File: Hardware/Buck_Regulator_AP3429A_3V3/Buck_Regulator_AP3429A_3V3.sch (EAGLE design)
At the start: 28 parts, among them J1 Screw Terminal, J2 POWER_JACKPOWER_JACK_SLOT_COM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, J3 Breakout Headers, U1 AP3429/A

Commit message: Updates from design review
Restructured file folder and project structure to have design files with two different eagle projects within the same github folder; adjusted components on layout for better loop stability; moved indicator for which version of the board to the bottom by the name; changed capacitor values to be better rated and size; added milling layer to power jack; adjusted thermals on output inductor; added more GND vias
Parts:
- 1.8V: value PROD_ID_PASTE_NO-SILK -> PROD_ID_NO-PASTE_NO_SILK; device SparkFun-Aesthetics:PROD_ID_PASTE_NO-SILK -> SparkFun-Aesthetics:PROD_ID_NO-PASTE_NO_SILK
- 3.3V: value PROD_ID_NO-PASTE_NO_SILK -> PROD_ID_PASTE_NO-SILK; device SparkFun-Aesthetics:PROD_ID_NO-PASTE_NO_SILK -> SparkFun-Aesthetics:PROD_ID_PASTE_NO-SILK
- C1, C3, C4: device SparkFun-Capacitors:22UF-0603-6.3V-20% -> SparkFun-Capacitors:22UF-0805-16V-20%
- R1: value 300k -> 453k; device SparkFun-Resistors:300KOHM-0603-1/10W-1% -> SparkFun-Resistors:453KOHM-0603-1/10W-1%
- R2: value 150k -> 100k; device SparkFun-Resistors:150KOHM-0603-1/10W-1% -> SparkFun-Resistors:100KOHM-0603-1/10W-1%
- R3: value 100 -> 1k; device SparkFun-Resistors:100OHM-0603-1/10W-1% -> SparkFun-Resistors:1KOHM-0603-1/10W-1%
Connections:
- net 1.8V renamed VOUT
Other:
- note added: "Adjustable DC-DC Buck Regulator - AP3429/A"
- note added: "Input Range: 3.9V to 5.5V"
- note added: "Output Voltage: 3.3V"
- note removed: "1.8V DC-DC Buck Regulator - AP3429/A"
- note removed: "1.8V Output, Use R1 = 300k and R2 = 150k 3.3V Output, Use R1 = 450k and R2 = 100k"
- note removed: "1.8V Output, Use R3 = 100 3.3V Output, Use R3 = 1k"
- note removed: "Input Range: 2.7V to 5V"

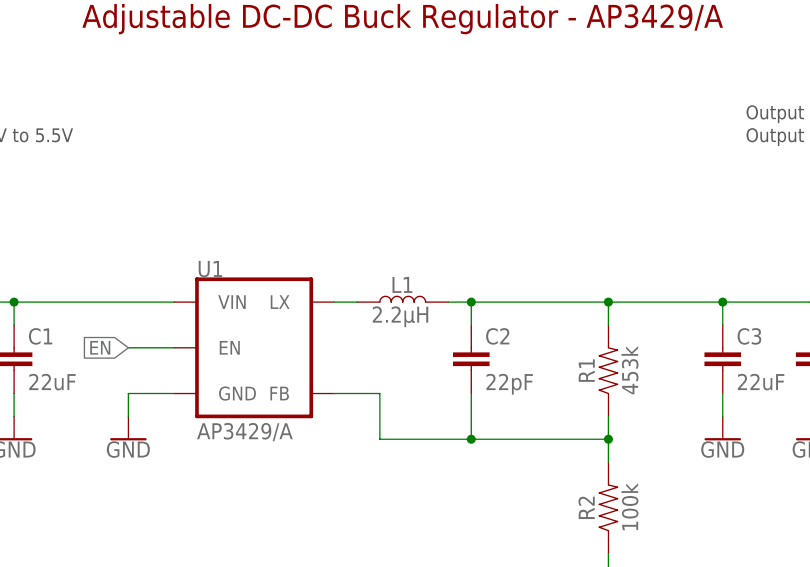
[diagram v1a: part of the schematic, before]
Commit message: Updated 3.3V files to be the same as 1.8V
Changed the 3 resistors (R1, R2, R3) and placed them in the same location as the 1.8V board files.
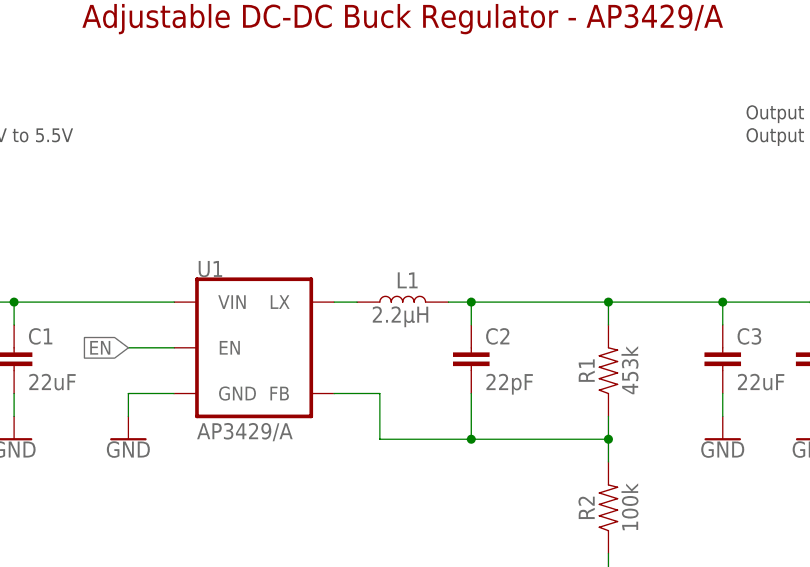
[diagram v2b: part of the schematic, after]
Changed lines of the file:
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@@
 </instance>
 <instance part="L1" gate="L1" x="66.04" y="109.22" smashed="yes" rot="R90">
-<attribute name="NAME" x="67.31" y="112.014" size="1.778" layer="95" font="vector" rot="R180"/>
+<attribute name="NAME" x="65.278" y="110.744" size="1.778" layer="95" font="vector" rot="R180" align="top-right"/>
 <attribute name="VALUE" x="69.088" y="106.934" size="1.778" layer="96" font="vector" rot="R180" align="top-left"/>
 </instance>

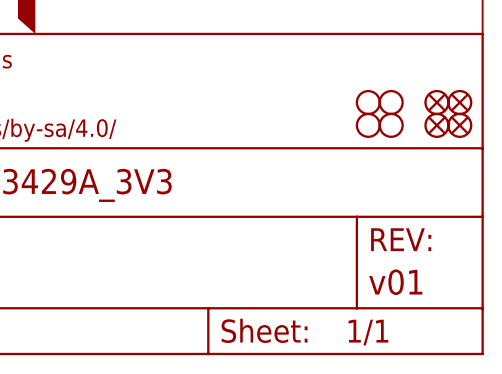
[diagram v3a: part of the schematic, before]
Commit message: Changed version number in schematic, adjusted components
Moved around some silkscreen in order for easier reading on the backside; changed the version number in the schematic to v10
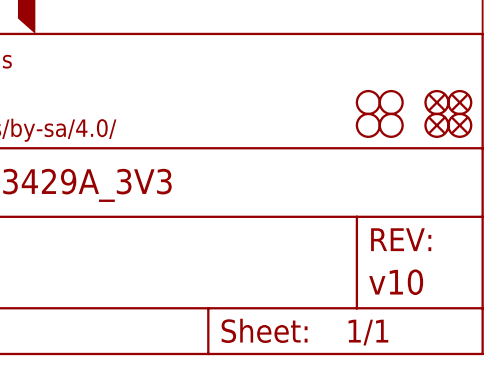
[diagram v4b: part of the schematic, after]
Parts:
- FRAME1: REV v01 -> v10
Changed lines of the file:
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@@
 <part name="FRAME1" library="SparkFun-Aesthetics" deviceset="FRAME-LEDGER" device="">
 <attribute name="DESIGNER" value="M. Chodikov"/>
-<attribute name="REV" value="v01"/>
+<attribute name="REV" value="v10"/>
 </part>
 <part name="FD1" library="SparkFun-Aesthetics" deviceset="FIDUCIAL" device="UFIDUCIAL"/>

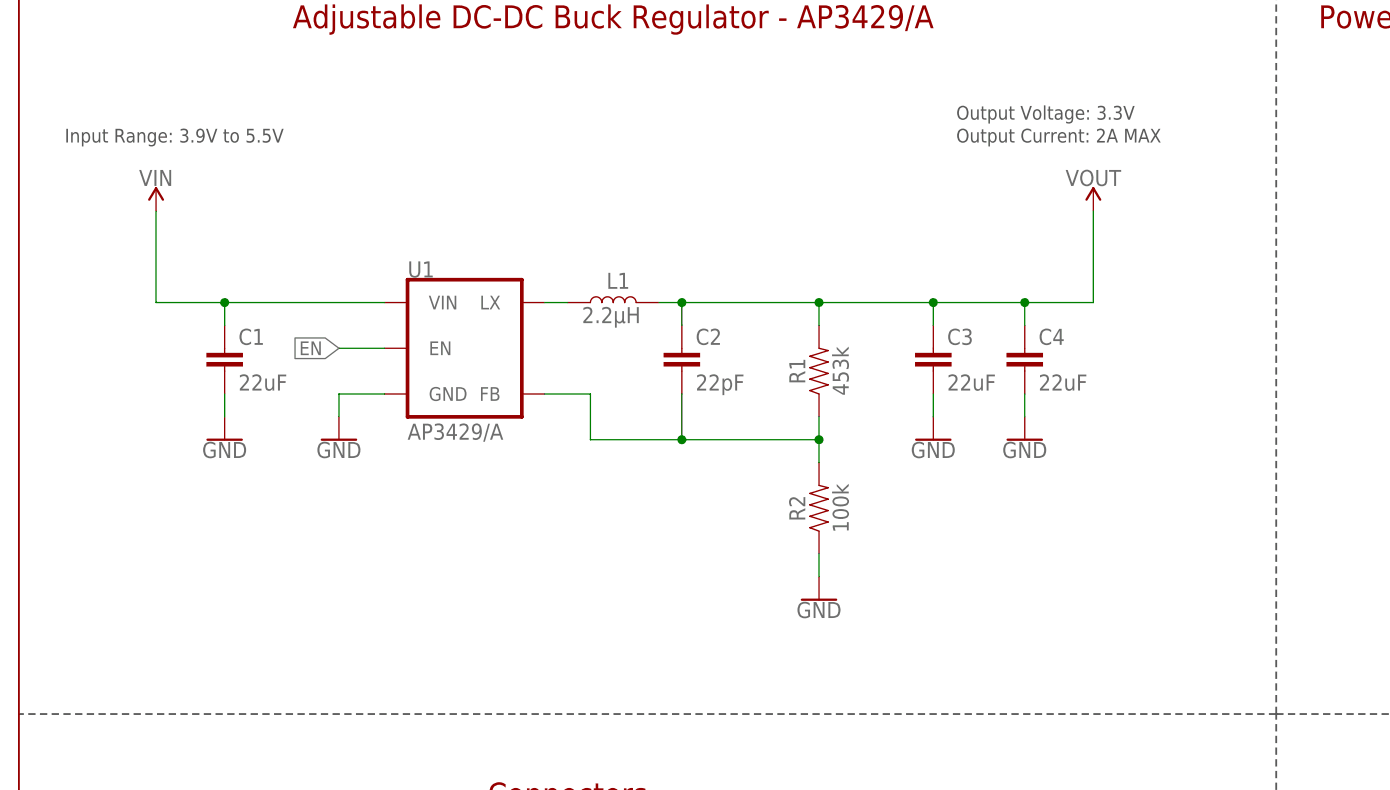
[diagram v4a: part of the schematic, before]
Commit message: Added 2 more output capacitors
Added more output capacitance to match ALC block - there was some ripple detected during testing so adding these should eliminate that. Adjusted the components on the board accordingly then matched the exact locations of said movement for each board.
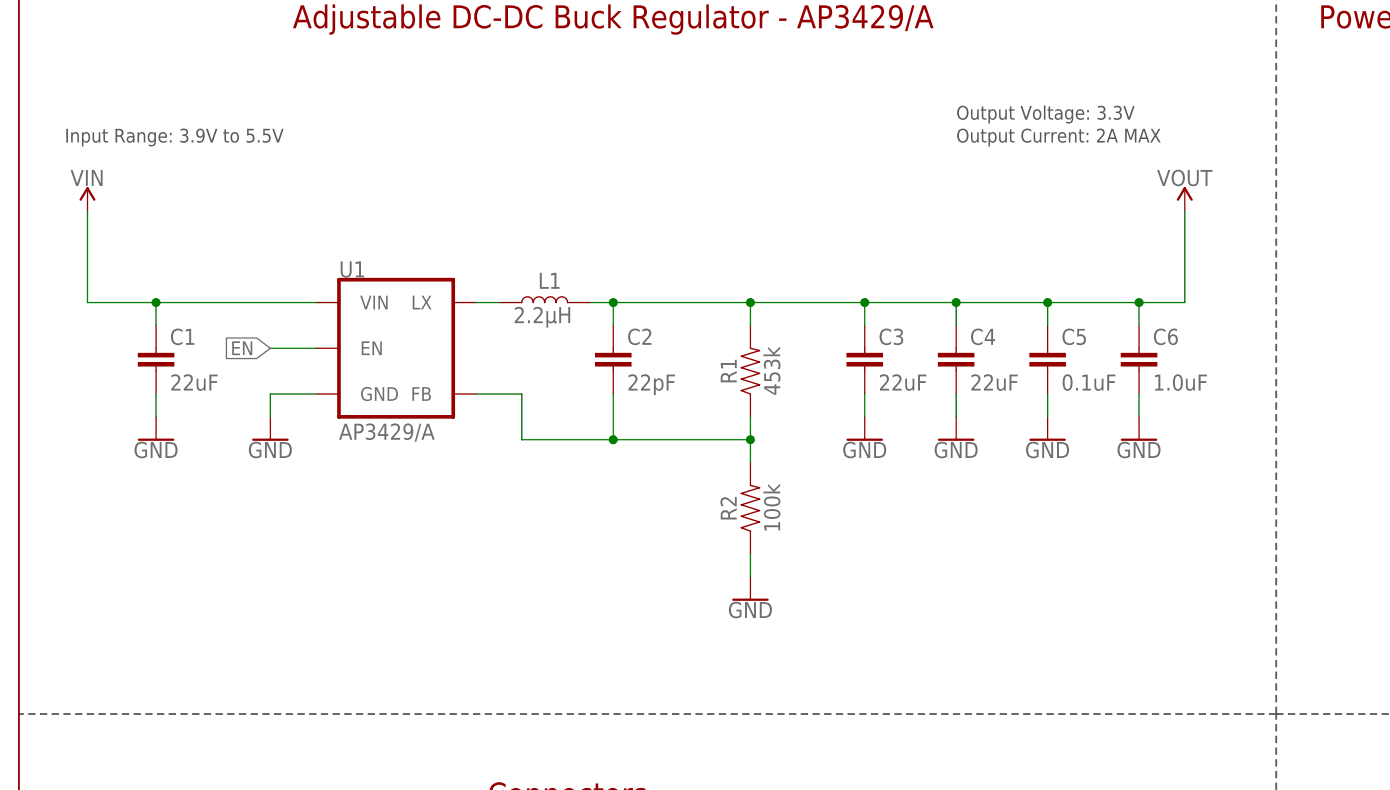
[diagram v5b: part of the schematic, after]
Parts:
- added C5: 0.1uF, SparkFun-Capacitors:0.1UF-0603-25V-5%
- added C6: 1.0uF, SparkFun-Capacitors:1.0UF-0603-16V-10%-X7R
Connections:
- net GND: now also C5.2, C6.2
- net VOUT: now also C5.1, C6.1
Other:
- moved on the sheet: C1, C2, C3, C4, L1, R1, R2, U1

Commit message: Design Review changes
Cleaned up 1.8V Hardware folder by deleting unneeded files, adjusted schematic notes for easier reading, deleted extraneous measures, adjusted GND via sizes to be the same size (15mil), adjusted some vias for better GND plane connection
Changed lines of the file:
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@@
 <sheet>
 <plain>
-<text x="5.08" y="127" size="1.524" layer="97" font="vector">Input Range: 3.9V to 5.5V</text>
+<text x="53.34" y="137.16" size="1.524" layer="97" font="vector">Input Range: 3.9V to 5.5V</text>
 <wire x1="0" y1="0" x2="139.7" y2="0" width="0.2032" layer="94"/>
 <wire x1="241.3" y1="35.56" x2="241.3" y2="149.86" width="0.2032" layer="94"/>
@@
 <wire x1="139.7" y1="63.5" x2="0" y2="63.5" width="0.2032" layer="97" style="longdash"/>
 <text x="58.42" y="37.084" size="1.524" layer="97" font="vector">POWER_JACK</text>
-<text x="104.14" y="127" size="1.524" layer="97" font="vector">Output Current: 2A MAX</text>
+<text x="53.34" y="132.08" size="1.524" layer="97" font="vector">Output Current: 2A MAX</text>
 <text x="45.72" y="5.08" size="1.524" layer="97" font="vector">WARNING: Only connect one Vin input at a time</text>
 <wire x1="139.7" y1="63.5" x2="139.7" y2="149.86" width="0.2032" layer="97" style="longdash"/>
@@
 to disconnect
 LED.</text>
-<text x="104.14" y="129.54" size="1.524" layer="97" font="vector">Output Voltage: 3.3V</text>
+<text x="55.88" y="134.62" size="1.524" layer="97" font="vector">Output Voltage: 3.3V</text>
 </plain>
 <instances>

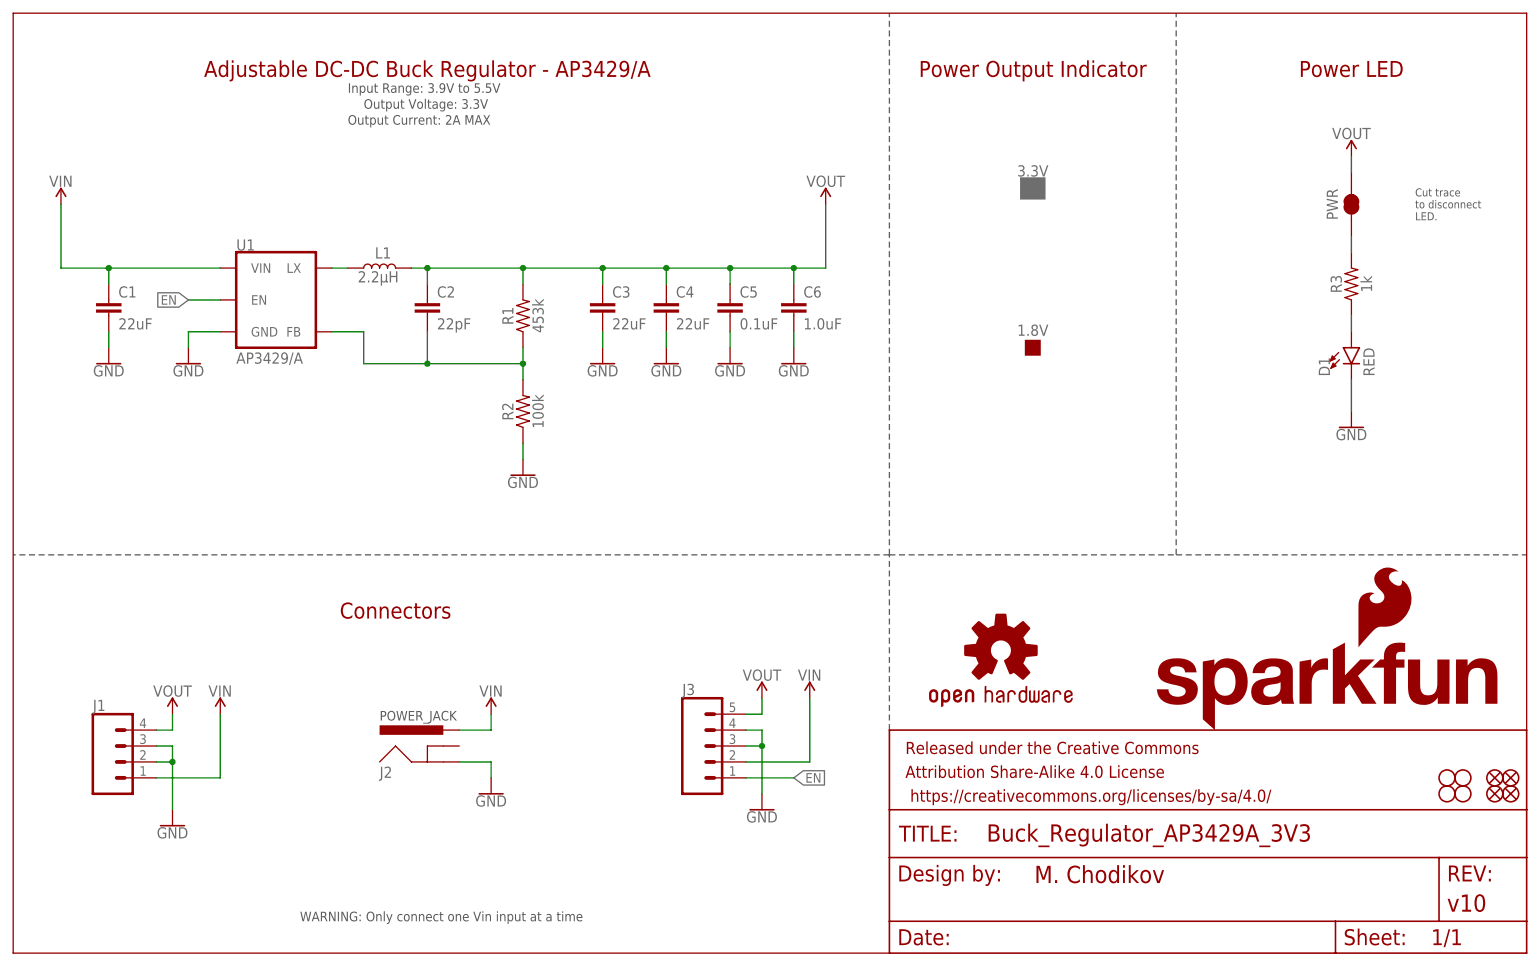
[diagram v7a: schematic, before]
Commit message: V11 Design Update
Added 100k resistor to pull EN high to VIN for an easier plug and play application.
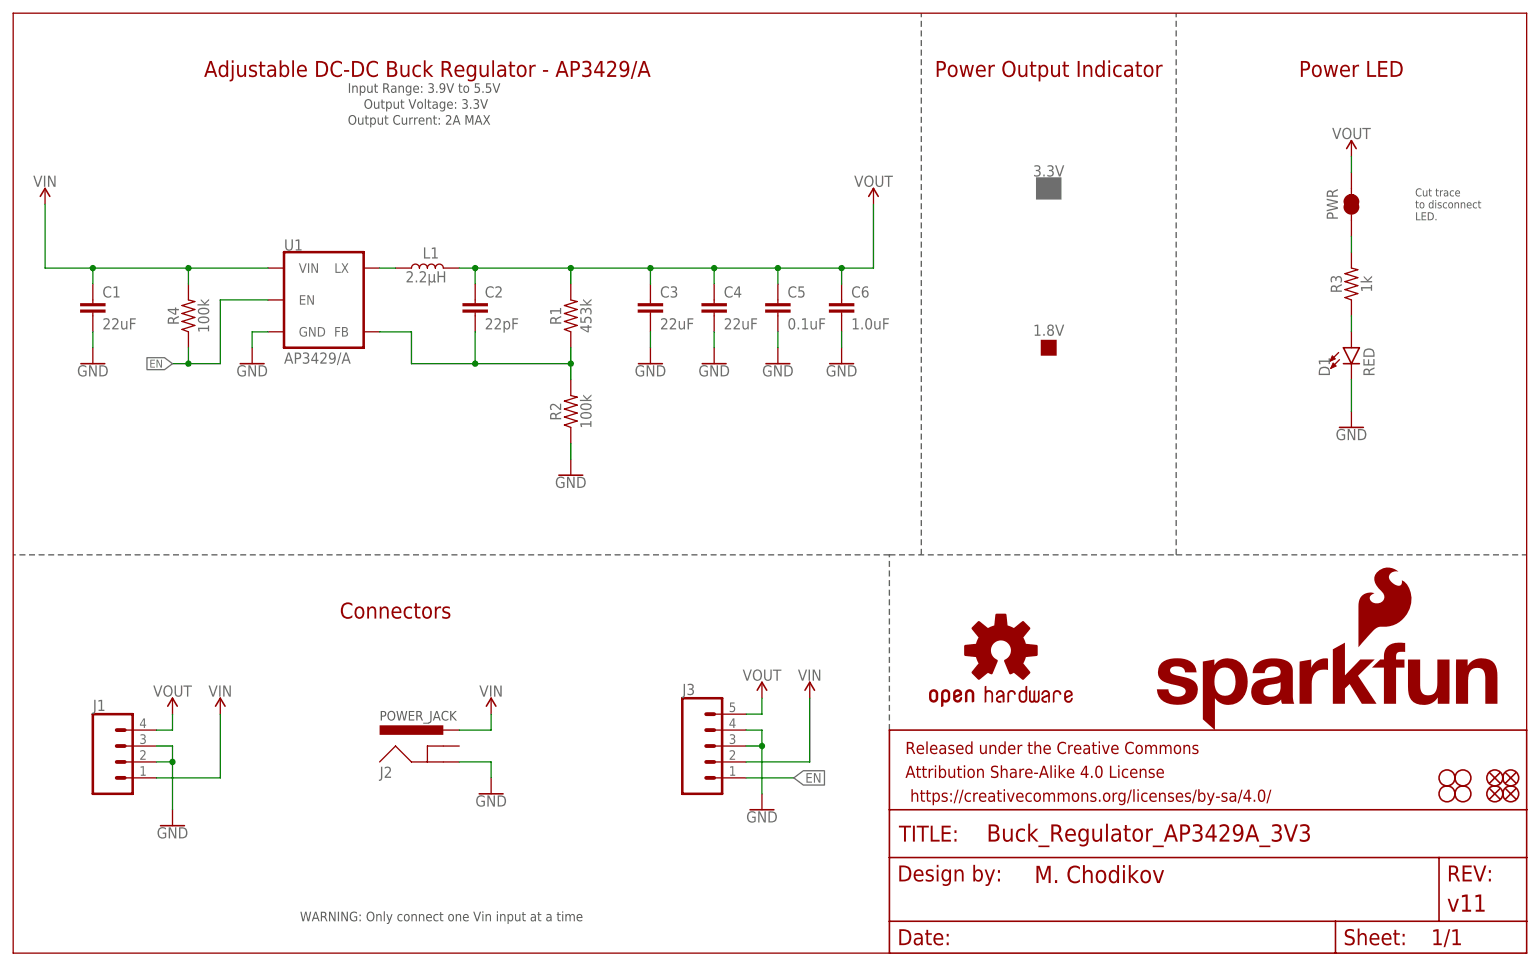
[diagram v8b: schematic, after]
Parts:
- added R4: 100k, SparkFun-Resistors:100KOHM-0603-1/10W-1%
- FRAME1: REV v10 -> v11
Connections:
- net EN: now also R4.1
- net VIN: now also R4.2
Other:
- moved on the sheet: 1.8V, 3.3V, C1, C2, C3, C4, C5, C6, L1, R1, R2, U1
